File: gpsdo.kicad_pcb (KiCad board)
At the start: 2 copper layers, 202 parts, among them J1 OLED, J10 10MHZ_OUT, J11 100MHZ_OUT, J12 10MHZ_OUT, J13 10MHZ_OUT, J14 10MHZ_OUT, J15 10MHZ_OUT, J16 LED, J17 TIMEPULSE, J18 TAP_GPS_TX, J19 TAP_GPS_RX, J2 ARDUINO_UART, J20 TAP_DAC_SDA, J21 TAP_DAC_SCL, J22 TAP_GPS_RF_IN, J23 TAP_GPS_TPLS, J24 TAP_GPS_V_ANT, J3 VOLTMETER, J4 ARDUINO_EXTRA_PINS, J5 POWER_IN, J6 GPS_ANT, J7 10MHZ_OUT, J8 10MHZ_OUT, J9 10MHZ_OUT, U1 TPS79301-EP, U10 MSA-0385, U11 MSA-0385, U12 MSA-0385, U13 MSA-0385, U14 MSA-0385, U15 MSA-0385, U16 MSA-0385, U17 MSA-0385, U18 MSA-0385, U19 MSA-0385, U2 TPS79301-EP, U20 MSA-0385, U21 TPS7A4501DCQT, U3 TPS7A4501DCQT, U4 SN74HC244, U5 DAC8571IDGKR, U6 LEA-M8F, U7 CVSS-945, U8 SN74HC541DWR, U9 MC12080

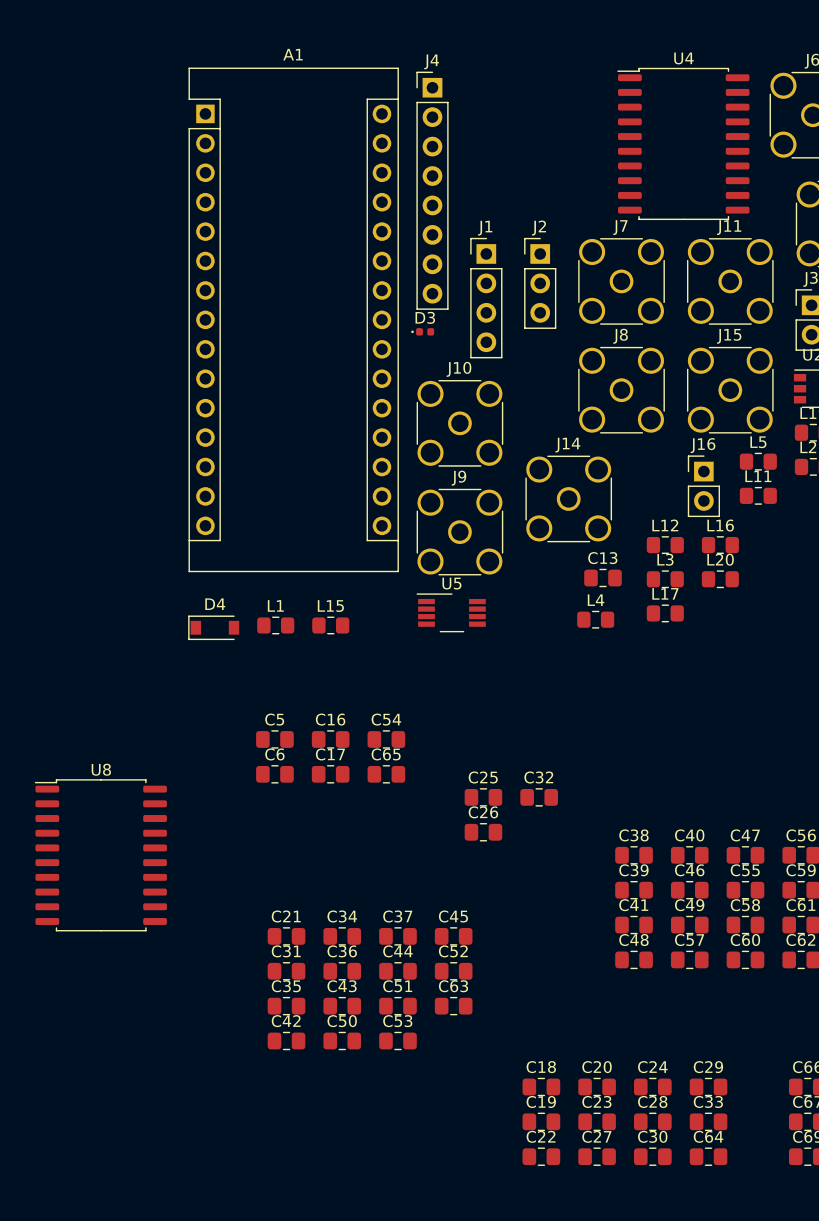
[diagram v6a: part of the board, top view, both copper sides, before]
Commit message: Updated U4 to 541
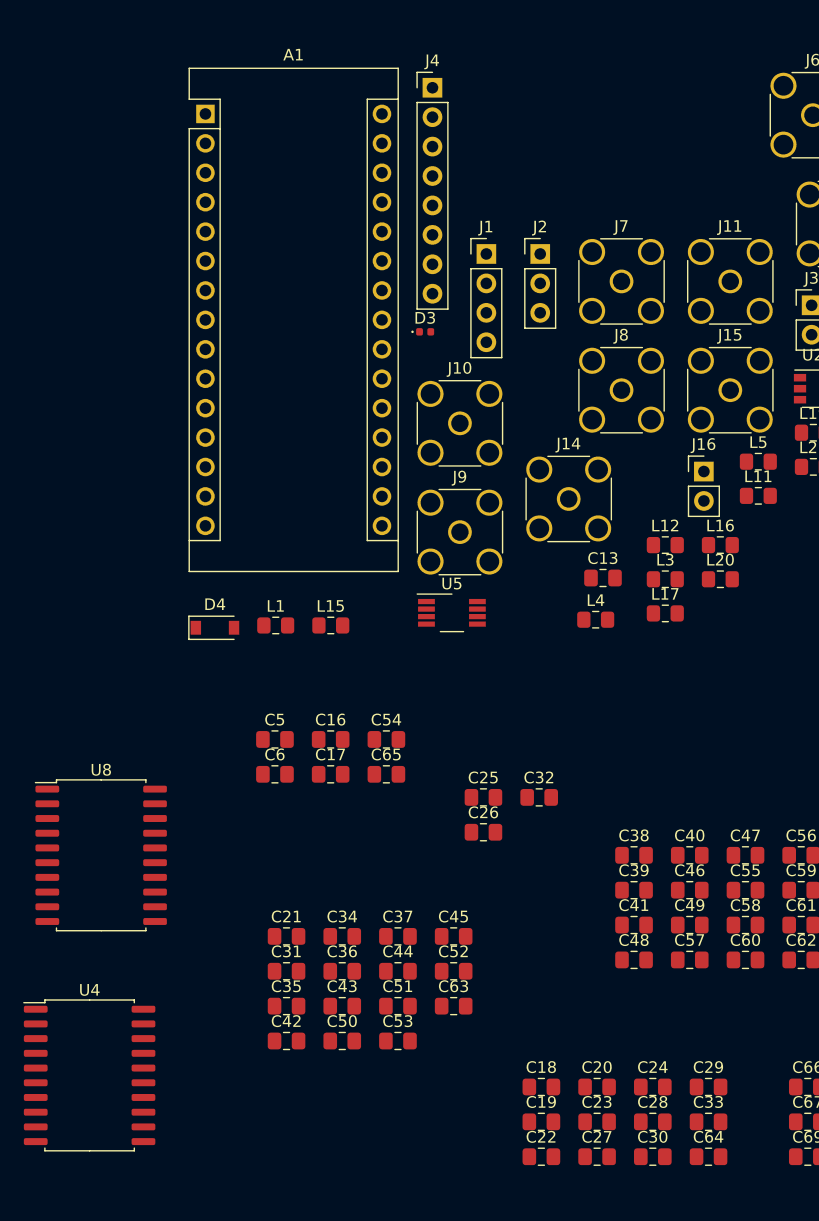
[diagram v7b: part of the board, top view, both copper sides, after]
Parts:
- U4: value SN74HC244 -> SN74HC541DWR
- moved U4 95.4 mm to (48.0, 122.0)
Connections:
- U4 pad 12: GPS_RF_IN -> (no net)
- U4 pad 14: TIMEPULSE -> (no net)
- U4 pad 15: (no net) -> GPS_RF_IN
- U4 pad 16: Net-(D4-Pad1) -> TIMEPULSE
- U4 pad 17: (no net) -> Net-(D4-Pad1)
- U4 pad 3: (no net) -> GPS_TX
- U4 pad 4: GPS_TX -> GPS_TPLS
- U4 pad 5: (no net) -> Net-(C1-Pad2)
- U4 pad 6: GPS_TPLS -> (no net)
- U4 pad 8: Net-(C1-Pad2) -> (no net)

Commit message: first_layout
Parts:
- moved J18 215.1 mm to (27.2, 191.0)
- moved J19 215.1 mm to (31.9, 191.0)
- moved J20 215.1 mm to (27.2, 195.6)
- moved J21 215.1 mm to (31.9, 195.6)
- moved J22 215.1 mm to (36.5, 191.0)
- moved J23 215.1 mm to (27.2, 200.3)
- moved J24 215.1 mm to (31.9, 200.3)
- moved R38 178.9 mm to (27.2, 47.0), turned to 180 degrees
- moved R42 160.0 mm to (27.2, 125.5), turned to 180 degrees
- moved R39 159.0 mm to (27.2, 63.5), turned to 180 degrees
- moved R40 157.4 mm to (27.2, 84.1), turned to 180 degrees
- moved R29 151.7 mm to (27.2, 134.6), turned to 180 degrees
- moved J6 147.2 mm to (20.3, 155.4)
- moved R26 146.8 mm to (27.2, 73.7), turned to 180 degrees
- moved U20 146.8 mm to (34.3, 130.8), turned to 90 degrees
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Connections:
- A1 pad 15: (no net) -> Net-(A1-Pad15)
- A1 pad 17: (no net) -> Net-(A1-Pad17)
- A1 pad 18: (no net) -> Net-(A1-Pad18)
- A1 pad 19: (no net) -> Net-(A1-Pad19)
- A1 pad 20: (no net) -> Net-(A1-Pad20)
- A1 pad 21: (no net) -> Net-(A1-Pad21)
- A1 pad 22: (no net) -> Net-(A1-Pad22)
- A1 pad 25: (no net) -> Net-(A1-Pad25)
- A1 pad 26: (no net) -> Net-(A1-Pad26)
- A1 pad 28: (no net) -> Net-(A1-Pad28)
- A1 pad 3: (no net) -> Net-(A1-Pad3)
- C68 pad 1: V_MMIC -> GND
- C69 pad 1: V_MMIC -> GND
- C72 pad 1: V_MMIC -> GND
- C73 pad 1: V_MMIC -> GND
- C76 pad 1: V_MMIC -> GND
- C77 pad 1: V_MMIC -> GND
- R15 pad 2: V_ARDUINO -> Net-(C26-Pad2)
- R35 pad 1: /A5_IN -> /A6_IN
- R36 pad 1: /A2_IN -> /A3_IN
- R37 pad 1: /A6_IN -> /A5_IN
- R43 pad 1: /A3_IN -> /A2_IN
- R44 pad 1: /A7_IN -> /A8_IN
- R46 pad 1: /A8_IN -> /A7_IN
- U4 pad 11: (no net) -> Net-(U4-Pad11)
- U4 pad 12: (no net) -> Net-(U4-Pad12)
- U4 pad 13: (no net) -> Net-(U4-Pad13)
- U4 pad 14: (no net) -> Net-(U4-Pad14)
- U4 pad 6: (no net) -> Net-(U4-Pad6)
- U4 pad 7: (no net) -> Net-(U4-Pad7)
- U4 pad 8: (no net) -> Net-(U4-Pad8)
- U4 pad 9: (no net) -> Net-(U4-Pad9)
- U6 pad 1: (no net) -> Net-(U6-Pad1)
- U6 pad 10: (no net) -> Net-(U6-Pad10)
- U6 pad 12: (no net) -> Net-(U6-Pad12)
- U6 pad 2: (no net) -> Net-(U6-Pad2)
- U6 pad 20: (no net) -> Net-(U6-Pad20)
- U6 pad 24: (no net) -> Net-(U6-Pad24)
- U6 pad 25: (no net) -> Net-(U6-Pad25)
- U6 pad 26: (no net) -> Net-(U6-Pad26)
- U6 pad 27: (no net) -> Net-(U6-Pad27)
- U6 pad 5: (no net) -> Net-(U6-Pad5)
- U6 pad 8: (no net) -> Net-(U6-Pad8)
- U6 pad 9: (no net) -> Net-(U6-Pad9)
- U8 pad 11: (no net) -> Net-(U8-Pad11)
- U8 pad 12: (no net) -> Net-(U8-Pad12)
- U8 pad 13: (no net) -> Net-(U8-Pad13)
- U8 pad 14: (no net) -> Net-(U8-Pad14)
- U8 pad 6: (no net) -> Net-(U8-Pad6)
- U8 pad 7: (no net) -> Net-(U8-Pad7)
- U8 pad 8: (no net) -> Net-(U8-Pad8)
- U8 pad 9: (no net) -> Net-(U8-Pad9)
